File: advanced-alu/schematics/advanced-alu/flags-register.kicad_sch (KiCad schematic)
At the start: 2 parts

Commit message: updated ALU design
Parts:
- added U?: 74LS04, symbol 74xx:74LS04
- added U?: 74LS245, symbol 74xx:74LS245
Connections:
- net CF: now also U?.3 (A1)
- net EF: now also U?.5 (A3)
- net GND: now also U?.10 (GND), U?.6 (A4), U?.7 (A5), U?.8 (A6), U?.9 (A7)
- net OF: now also U?.4 (A2)
- net VCC: now also U?.1 (A->B), U?.20 (VCC)
- net ZF: now also U?.2 (A0)
- net ∑f renamed ALUf
- new net: U?.19 (CE), U?.2
- new net BUS_0: U?.18 (B0)
- new net BUS_1: U?.17 (B1)
- new net BUS_2: U?.16 (B2)
- new net BUS_3: U?.15 (B3)
- new net BUS_4: U?.14 (B4)
- new net BUS_5: U?.13 (B5)
- new net BUS_6: U?.12 (B6)
- new net BUS_7: U?.11 (B7)
- new net Fo: U?.1

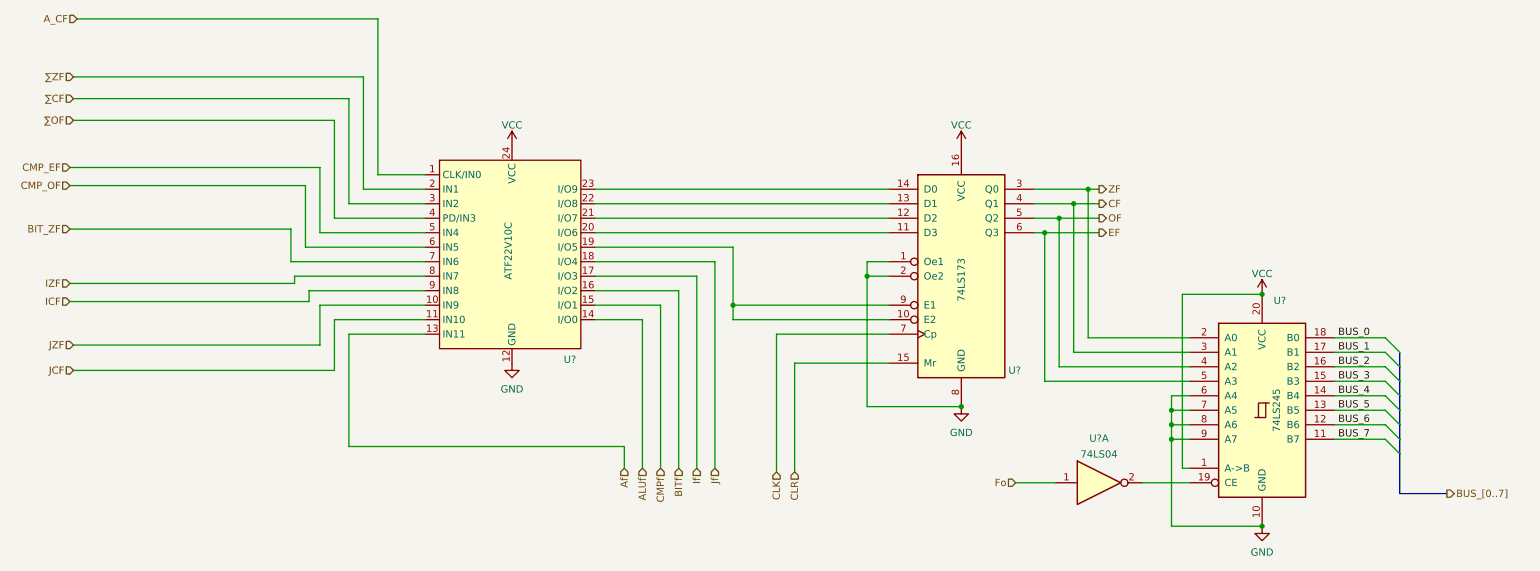
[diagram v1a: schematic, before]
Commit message: updated flags register
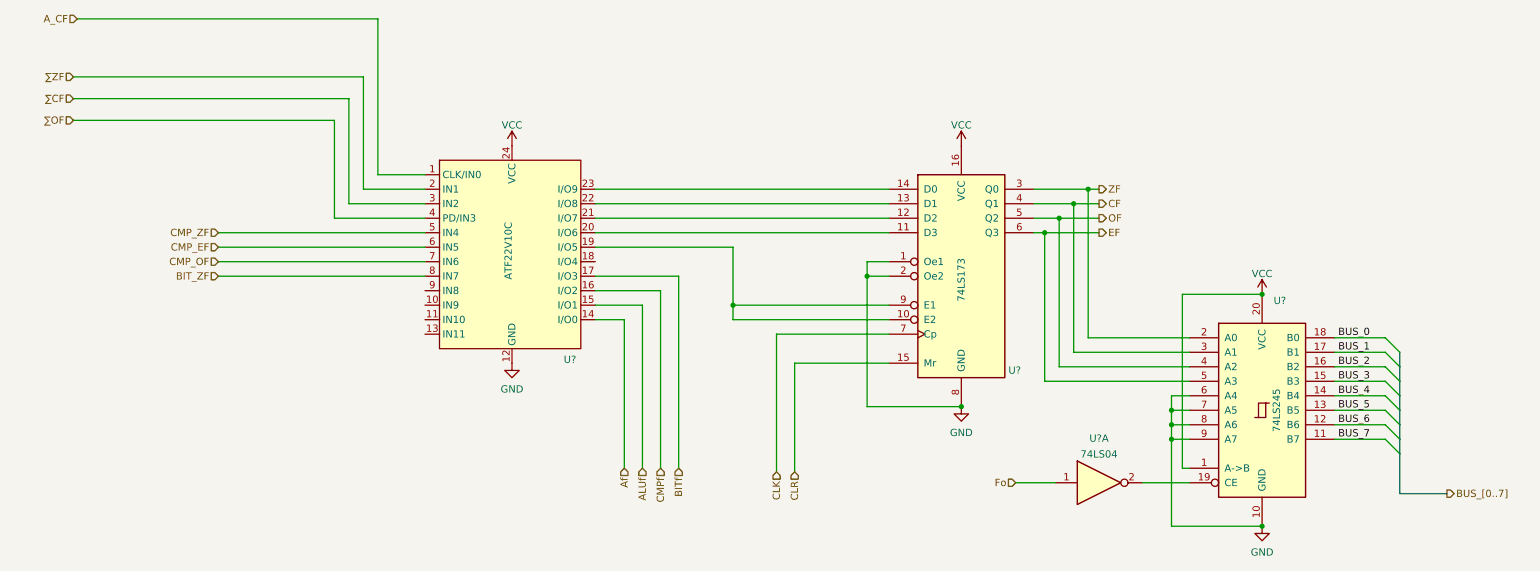
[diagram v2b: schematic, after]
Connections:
- net IZF is gone; now on net BIT_ZF: U?.8 (IN7)
- net If is gone; now on net BITf: U?.17 (I/O3)
- net ALUf: now also U?.15 (I/O1); no longer U?.14 (I/O0)
- net Af: now also U?.14 (I/O0); no longer U?.13 (IN11)
- net BIT_ZF: no longer U?.7 (IN6)
- net BITf: no longer U?.16 (I/O2)
- net CMP_EF: now also U?.6 (IN5); no longer U?.5 (IN4)
- net CMP_OF: now also U?.7 (IN6); no longer U?.6 (IN5)
- net CMPf: now also U?.16 (I/O2); no longer U?.15 (I/O1)
- net ICF: no longer names the net of U?.9 (IN8)
- net JCF: no longer names the net of U?.11 (IN10)
- net JZF: no longer names the net of U?.10 (IN9)
- net Jf: no longer names the net of U?.18 (I/O4)
- new net CMP_ZF: U?.5 (IN4)

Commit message: updated documentation
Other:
- title: (none) -> Advanced Arithmetic Logic Unit - Flags Register
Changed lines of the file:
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@@
 (kicad_sch (version 20211123) (generator eeschema)
   (paper "A4")
+  (title_block
+    (title "Advanced Arithmetic Logic Unit - Flags Register")
+  )
   (junction (at 217.17 119.38) (diameter 0) (color 0 0 0 0)
   )

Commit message: returned temp registr to being 8-bit
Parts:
- gave numbers to parts that had none: 4
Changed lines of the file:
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@@
   (symbol (lib_id "74xx:74LS04") (at 204.47 127 0) (unit 1)
     (in_bom yes) (on_board yes) (fields_autoplaced)
-    (property "Reference" "U?" (id 0) (at 204.47 119.2235 0))
+    (property "Reference" "U26" (id 0) (at 204.47 119.2235 0))
     (property "Value" "74LS04" (id 1) (at 204.47 121.9986 0))
     (property "Footprint" "" (id 2) (at 204.47 127 0)
@@
   (symbol (lib_id "power:GND") (at 101.6 106.045 0) (unit 1)
     (in_bom yes) (on_board yes) (fields_autoplaced)
-    (property "Reference" "#PWR?" (id 0) (at 101.6 112.395 0)
+    (property "Reference" "#PWR030" (id 0) (at 101.6 112.395 0)
       (effects (font (size 1.27 1.27)) hide)
     )
@@
   (symbol (lib_id "power:VCC") (at 233.045 93.98 0) (unit 1)
     (in_bom yes) (on_board yes) (fields_autoplaced)
-    (property "Reference" "#PWR?" (id 0) (at 233.045 97.79 0)
+    (property "Reference" "#PWR033" (id 0) (at 233.045 97.79 0)
       (effects (font (size 1.27 1.27)) hide)
     )
@@
   (symbol (lib_id "power:GND") (at 180.34 113.665 0) (unit 1)
     (in_bom yes) (on_board yes) (fields_autoplaced)
-    (property "Reference" "#PWR?" (id 0) (at 180.34 120.015 0)
+    (property "Reference" "#PWR032" (id 0) (at 180.34 120.015 0)
       (effects (font (size 1.27 1.27)) hide)
     )
@@
   (symbol (lib_id "power:GND") (at 233.045 134.62 0) (unit 1)
     (in_bom yes) (on_board yes) (fields_autoplaced)
-    (property "Reference" "#PWR?" (id 0) (at 233.045 140.97 0)
+    (property "Reference" "#PWR034" (id 0) (at 233.045 140.97 0)
       (effects (font (size 1.27 1.27)) hide)
     )
@@
   (symbol (lib_id "power:VCC") (at 101.6 67.945 0) (unit 1)
     (in_bom yes) (on_board yes) (fields_autoplaced)
-    (property "Reference" "#PWR?" (id 0) (at 101.6 71.755 0)
+    (property "Reference" "#PWR029" (id 0) (at 101.6 71.755 0)
       (effects (font (size 1.27 1.27)) hide)
     )
@@
   (symbol (lib_id "74xx:74LS173") (at 180.34 90.805 0) (unit 1)
     (in_bom yes) (on_board yes)
-    (property "Reference" "U?" (id 0) (at 188.595 107.315 0)
+    (property "Reference" "U25" (id 0) (at 188.595 107.315 0)
       (effects (font (size 1.27 1.27)) (justify left))
     )
@@
   (symbol (lib_id "power:VCC") (at 180.34 67.945 0) (unit 1)
     (in_bom yes) (on_board yes) (fields_autoplaced)
-    (property "Reference" "#PWR?" (id 0) (at 180.34 71.755 0)
+    (property "Reference" "#PWR031" (id 0) (at 180.34 71.755 0)
       (effects (font (size 1.27 1.27)) hide)
     )
@@
   (symbol (lib_id "74xx:74LS245") (at 233.045 114.3 0) (unit 1)
     (in_bom yes) (on_board yes)
-    (property "Reference" "U?" (id 0) (at 235.0644 95.0935 0)
+    (property "Reference" "U27" (id 0) (at 235.0644 95.0935 0)
       (effects (font (size 1.27 1.27)) (justify left))
     )
@@
   (symbol (lib_id "common-symbols:ATF22V10C") (at 101.6 86.995 0) (unit 1)
     (in_bom yes) (on_board yes)
-    (property "Reference" "U?" (id 0) (at 111.76 105.41 0))
+    (property "Reference" "U24" (id 0) (at 111.76 105.41 0))
     (property "Value" "ATF22V10C" (id 1) (at 100.965 86.36 90))
     (property "Footprint" "" (id 2) (at 101.6 86.995 0)

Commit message: small changes toimprove layout
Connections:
- net ALUf: now also U24.10 (IN9); no longer U24.15 (I/O1)
- net Af: now also U24.9 (IN8); no longer U24.14 (I/O0)
- net BITf: now also U24.13 (IN11); no longer U24.17 (I/O3)
- net CMPf: now also U24.11 (IN10); no longer U24.16 (I/O2)
- no-connect marks 0 -> 5
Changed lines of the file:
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@@
   (junction (at 217.17 116.84) (diameter 0) (color 0 0 0 0)
   )
+  (no_connect (at 116.205 88.265))
+  (no_connect (at 116.205 90.805))
+  (no_connect (at 116.205 93.345))
+  (no_connect (at 116.205 95.885))
+  (no_connect (at 116.205 98.425))
   (bus_entry (at 254.635 104.14) (size 2.54 2.54)
     (stroke (width 0) (type default) (color 0 0 0 0))
@@
     (stroke (width 0) (type default) (color 0 0 0 0))
   )
-  (wire (pts (xy 73.025 78.105) (xy 86.36 78.105))
+  (wire (pts (xy 50.165 78.105) (xy 86.36 78.105))
     (stroke (width 0) (type default) (color 0 0 0 0))
   )
@@
     (stroke (width 0) (type default) (color 0 0 0 0))
   )
-  (wire (pts (xy 70.485 80.645) (xy 86.36 80.645))
+  (wire (pts (xy 50.165 80.645) (xy 86.36 80.645))
     (stroke (width 0) (type default) (color 0 0 0 0))
   )
@@
     (stroke (width 0) (type default) (color 0 0 0 0))
   )
-  (wire (pts (xy 75.565 55.88) (xy 75.565 75.565))
+  (wire (pts (xy 50.165 98.425) (xy 86.36 98.425))
     (stroke (width 0) (type default) (color 0 0 0 0))
   )
@@
     (stroke (width 0) (type default) (color 0 0 0 0))
   )
-  (wire (pts (xy 130.81 90.805) (xy 130.81 124.46))
-    (stroke (width 0) (type default) (color 0 0 0 0))
-  )
-  (wire (pts (xy 24.765 55.88) (xy 75.565 55.88))
-    (stroke (width 0) (type default) (color 0 0 0 0))
-  )
   (wire (pts (xy 163.83 90.805) (xy 163.83 113.665))
     (stroke (width 0) (type default) (color 0 0 0 0))
@@
     (stroke (width 0) (type default) (color 0 0 0 0))
   )
+  (wire (pts (xy 50.165 100.965) (xy 86.36 100.965))
+    (stroke (width 0) (type default) (color 0 0 0 0))
+  )
   (wire (pts (xy 217.17 116.84) (xy 217.17 119.38))
     (stroke (width 0) (type default) (color 0 0 0 0))
@@
     (stroke (width 0) (type default) (color 0 0 0 0))
   )
-  (wire (pts (xy 127.635 93.345) (xy 127.635 124.46))
-    (stroke (width 0) (type default) (color 0 0 0 0))
-  )
   (wire (pts (xy 189.865 127) (xy 196.85 127))
     (stroke (width 0) (type default) (color 0 0 0 0))
   )
-  (wire (pts (xy 121.285 98.425) (xy 116.205 98.425))
-    (stroke (width 0) (type default) (color 0 0 0 0))
-  )
   (wire (pts (xy 220.345 124.46) (xy 219.075 124.46))
     (stroke (width 0) (type default) (color 0 0 0 0))
@@
     (stroke (width 0) (type default) (color 0 0 0 0))
   )
-  (wire (pts (xy 78.105 73.025) (xy 86.36 73.025))
+  (wire (pts (xy 50.165 73.025) (xy 86.36 73.025))
     (stroke (width 0) (type default) (color 0 0 0 0))
   )
@@
     (stroke (width 0) (type default) (color 0 0 0 0))
   )
-  (wire (pts (xy 121.285 98.425) (xy 121.285 124.46))
-    (stroke (width 0) (type default) (color 0 0 0 0))
-  )
   (wire (pts (xy 200.025 78.105) (xy 204.47 78.105))
     (stroke (width 0) (type default) (color 0 0 0 0))
@@
     (stroke (width 0) (type default) (color 0 0 0 0))
   )
-  (wire (pts (xy 73.025 59.69) (xy 73.025 78.105))
-    (stroke (width 0) (type default) (color 0 0 0 0))
-  )
   (bus (pts (xy 257.175 114.3) (xy 257.175 116.84))
     (stroke (width 0) (type default) (color 0 0 0 0))
@@
     (stroke (width 0) (type default) (color 0 0 0 0))
   )
-  (wire (pts (xy 24.765 63.5) (xy 70.485 63.5))
-    (stroke (width 0) (type default) (color 0 0 0 0))
-  )
-  (wire (pts (xy 124.46 95.885) (xy 116.205 95.885))
-    (stroke (width 0) (type default) (color 0 0 0 0))
-  )
   (wire (pts (xy 167.64 90.805) (xy 163.83 90.805))
     (stroke (width 0) (type default) (color 0 0 0 0))
   )
-  (wire (pts (xy 78.105 45.72) (xy 78.105 73.025))
-    (stroke (width 0) (type default) (color 0 0 0 0))
-  )
   (wire (pts (xy 220.345 116.84) (xy 217.17 116.84))
     (stroke (width 0) (type default) (color 0 0 0 0))
@@
     (stroke (width 0) (type default) (color 0 0 0 0))
   )
-  (wire (pts (xy 124.46 95.885) (xy 124.46 124.46))
-    (stroke (width 0) (type default) (color 0 0 0 0))
-  )
   (wire (pts (xy 219.075 124.46) (xy 219.075 93.98))
     (stroke (width 0) (type default) (color 0 0 0 0))
@@
     (stroke (width 0) (type default) (color 0 0 0 0))
   )
+  (wire (pts (xy 50.165 93.345) (xy 86.36 93.345))
+    (stroke (width 0) (type default) (color 0 0 0 0))
+  )
+  (wire (pts (xy 50.165 95.885) (xy 86.36 95.885))
+    (stroke (width 0) (type default) (color 0 0 0 0))
+  )
   (wire (pts (xy 116.205 75.565) (xy 167.64 75.565))
     (stroke (width 0) (type default) (color 0 0 0 0))
   )
-  (wire (pts (xy 127.635 93.345) (xy 116.205 93.345))
-    (stroke (width 0) (type default) (color 0 0 0 0))
-  )
   (wire (pts (xy 245.745 109.22) (xy 254.635 109.22))
     (stroke (width 0) (type default) (color 0 0 0 0))
   )
-  (wire (pts (xy 24.765 59.69) (xy 73.025 59.69))
-    (stroke (width 0) (type default) (color 0 0 0 0))
-  )
-  (wire (pts (xy 130.81 90.805) (xy 116.205 90.805))
-    (stroke (width 0) (type default) (color 0 0 0 0))
-  )
   (bus (pts (xy 257.175 106.68) (xy 257.175 109.22))
     (stroke (width 0) (type default) (color 0 0 0 0))
   )
-  (wire (pts (xy 75.565 75.565) (xy 86.36 75.565))
-    (stroke (width 0) (type default) (color 0 0 0 0))
-  )
-  (wire (pts (xy 25.4 45.72) (xy 78.105 45.72))
+  (wire (pts (xy 50.165 75.565) (xy 86.36 75.565))
     (stroke (width 0) (type default) (color 0 0 0 0))
   )
@@
     (stroke (width 0) (type default) (color 0 0 0 0))
   )
-  (wire (pts (xy 70.485 63.5) (xy 70.485 80.645))
-    (stroke (width 0) (type default) (color 0 0 0 0))
-  )
   (label "BUS_4" (at 246.38 111.76 0)
     (effects (font (size 1.27 1.27)) (justify left bottom))
@@
     (effects (font (size 1.27 1.27)) (justify left))
   )
-  (hierarchical_label "A_CF" (shape input) (at 25.4 45.72 180)
-    (effects (font (size 1.27 1.27)) (justify right))
-  )
-  (hierarchical_label "∑ZF" (shape input) (at 24.765 55.88 180)
+  (hierarchical_label "A_CF" (shape input) (at 50.165 73.025 180)
+    (effects (font (size 1.27 1.27)) (justify right))
+  )
+  (hierarchical_label "∑ZF" (shape input) (at 50.165 75.565 180)
     (effects (font (size 1.27 1.27)) (justify right))
   )
@@
     (effects (font (size 1.27 1.27)) (justify left))
   )
-  (hierarchical_label "BITf" (shape input) (at 130.81 124.46 270)
+  (hierarchical_label "BITf" (shape input) (at 50.165 100.965 180)
     (effects (font (size 1.27 1.27)) (justify right))
   )
@@
     (effects (font (size 1.27 1.27)) (justify left))
   )
-  (hierarchical_label "Af" (shape input) (at 121.285 124.46 270)
-    (effects (font (size 1.27 1.27)) (justify right))
-  )
-  (hierarchical_label "CMPf" (shape input) (at 127.635 124.46 270)
+  (hierarchical_label "Af" (shape input) (at 50.165 93.345 180)
+    (effects (font (size 1.27 1.27)) (justify right))
+  )
+  (hierarchical_label "CMPf" (shape input) (at 50.165 98.425 180)
     (effects (font (size 1.27 1.27)) (justify right))
   )
@@
     (effects (font (size 1.27 1.27)) (justify right))
   )
-  (hierarchical_label "∑OF" (shape input) (at 24.765 63.5 180)
-    (effects (font (size 1.27 1.27)) (justify right))
-  )
-  (hierarchical_label "ALUf" (shape input) (at 124.46 124.46 270)
+  (hierarchical_label "∑OF" (shape input) (at 50.165 80.645 180)
+    (effects (font (size 1.27 1.27)) (justify right))
+  )
+  (hierarchical_label "ALUf" (shape input) (at 50.165 95.885 180)
     (effects (font (size 1.27 1.27)) (justify right))
   )
@@
     (effects (font (size 1.27 1.27)) (justify right))
   )
-  (hierarchical_label "∑CF" (shape input) (at 24.765 59.69 180)
+  (hierarchical_label "∑CF" (shape input) (at 50.165 78.105 180)
     (effects (font (size 1.27 1.27)) (justify right))
   )
@@
     (pin "1")
     (pin "2")
-    (pin "3")
-    (pin "4")
-    (pin "5")
-    (pin "6")
-    (pin "8")
-    (pin "9")
-    (pin "10")
-    (pin "11")
-    (pin "12")
-    (pin "13")
-    (pin "14")
-    (pin "7")
   )
   (symbol (lib_id "power:GND") (at 101.6 106.045 0) (unit 1)

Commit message: tweaks and layout improvements
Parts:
- renumbered U24 to U25, U25 to U26, U26 to U27, U27 to U28
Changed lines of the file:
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@@
   (symbol (lib_id "74xx:74LS04") (at 204.47 127 0) (unit 1)
     (in_bom yes) (on_board yes) (fields_autoplaced)
-    (property "Reference" "U26" (id 0) (at 204.47 119.2235 0))
+    (property "Reference" "U27" (id 0) (at 204.47 119.2235 0))
     (property "Value" "74LS04" (id 1) (at 204.47 121.9986 0))
     (property "Footprint" "" (id 2) (at 204.47 127 0)
@@
     (pin "1")
     (pin "2")
-    (pin "3")
-    (pin "4")
-    (pin "5")
-    (pin "6")
-    (pin "8")
-    (pin "9")
-    (pin "10")
-    (pin "11")
-    (pin "12")
-    (pin "13")
-    (pin "14")
-    (pin "7")
   )
   (symbol (lib_id "power:GND") (at 101.6 106.045 0) (unit 1)
     (in_bom yes) (on_board yes) (fields_autoplaced)
-    (property "Reference" "#PWR030" (id 0) (at 101.6 112.395 0)
+    (property "Reference" "#PWR034" (id 0) (at 101.6 112.395 0)
       (effects (font (size 1.27 1.27)) hide)
     )
@@
   (symbol (lib_id "power:VCC") (at 233.045 93.98 0) (unit 1)
     (in_bom yes) (on_board yes) (fields_autoplaced)
-    (property "Reference" "#PWR033" (id 0) (at 233.045 97.79 0)
+    (property "Reference" "#PWR037" (id 0) (at 233.045 97.79 0)
       (effects (font (size 1.27 1.27)) hide)
     )
@@
   (symbol (lib_id "power:GND") (at 180.34 113.665 0) (unit 1)
     (in_bom yes) (on_board yes) (fields_autoplaced)
-    (property "Reference" "#PWR032" (id 0) (at 180.34 120.015 0)
+    (property "Reference" "#PWR036" (id 0) (at 180.34 120.015 0)
       (effects (font (size 1.27 1.27)) hide)
     )
@@
   (symbol (lib_id "power:GND") (at 233.045 134.62 0) (unit 1)
     (in_bom yes) (on_board yes) (fields_autoplaced)
-    (property "Reference" "#PWR034" (id 0) (at 233.045 140.97 0)
+    (property "Reference" "#PWR038" (id 0) (at 233.045 140.97 0)
       (effects (font (size 1.27 1.27)) hide)
     )
@@
   (symbol (lib_id "power:VCC") (at 101.6 67.945 0) (unit 1)
     (in_bom yes) (on_board yes) (fields_autoplaced)
-    (property "Reference" "#PWR029" (id 0) (at 101.6 71.755 0)
+    (property "Reference" "#PWR033" (id 0) (at 101.6 71.755 0)
       (effects (font (size 1.27 1.27)) hide)
     )
@@
   (symbol (lib_id "74xx:74LS173") (at 180.34 90.805 0) (unit 1)
     (in_bom yes) (on_board yes)
-    (property "Reference" "U25" (id 0) (at 188.595 107.315 0)
+    (property "Reference" "U26" (id 0) (at 188.595 107.315 0)
       (effects (font (size 1.27 1.27)) (justify left))
     )
@@
   (symbol (lib_id "power:VCC") (at 180.34 67.945 0) (unit 1)
     (in_bom yes) (on_board yes) (fields_autoplaced)
-    (property "Reference" "#PWR031" (id 0) (at 180.34 71.755 0)
+    (property "Reference" "#PWR035" (id 0) (at 180.34 71.755 0)
       (effects (font (size 1.27 1.27)) hide)
     )
@@
   (symbol (lib_id "74xx:74LS245") (at 233.045 114.3 0) (unit 1)
     (in_bom yes) (on_board yes)
-    (property "Reference" "U27" (id 0) (at 235.0644 95.0935 0)
+    (property "Reference" "U28" (id 0) (at 235.0644 95.0935 0)
       (effects (font (size 1.27 1.27)) (justify left))
     )
@@
   (symbol (lib_id "common-symbols:ATF22V10C") (at 101.6 86.995 0) (unit 1)
     (in_bom yes) (on_board yes)
-    (property "Reference" "U24" (id 0) (at 111.76 105.41 0))
+    (property "Reference" "U25" (id 0) (at 111.76 105.41 0))
     (property "Value" "ATF22V10C" (id 1) (at 100.965 86.36 90))
     (property "Footprint" "" (id 2) (at 101.6 86.995 0)

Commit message: corrected control lines
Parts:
- renumbered U25 to U26, U26 to U27, U27 to U28, U28 to U29
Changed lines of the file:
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@@
   (symbol (lib_id "74xx:74LS04") (at 204.47 127 0) (unit 1)
     (in_bom yes) (on_board yes) (fields_autoplaced)
-    (property "Reference" "U27" (id 0) (at 204.47 119.2235 0))
+    (property "Reference" "U28" (id 0) (at 204.47 119.2235 0))
     (property "Value" "74LS04" (id 1) (at 204.47 121.9986 0))
     (property "Footprint" "" (id 2) (at 204.47 127 0)
@@
   (symbol (lib_id "74xx:74LS173") (at 180.34 90.805 0) (unit 1)
     (in_bom yes) (on_board yes)
-    (property "Reference" "U26" (id 0) (at 188.595 107.315 0)
+    (property "Reference" "U27" (id 0) (at 188.595 107.315 0)
       (effects (font (size 1.27 1.27)) (justify left))
     )
@@
   (symbol (lib_id "74xx:74LS245") (at 233.045 114.3 0) (unit 1)
     (in_bom yes) (on_board yes)
-    (property "Reference" "U28" (id 0) (at 235.0644 95.0935 0)
+    (property "Reference" "U29" (id 0) (at 235.0644 95.0935 0)
       (effects (font (size 1.27 1.27)) (justify left))
     )
@@
   (symbol (lib_id "common-symbols:ATF22V10C") (at 101.6 86.995 0) (unit 1)
     (in_bom yes) (on_board yes)
-    (property "Reference" "U25" (id 0) (at 111.76 105.41 0))
+    (property "Reference" "U26" (id 0) (at 111.76 105.41 0))
     (property "Value" "ATF22V10C" (id 1) (at 100.965 86.36 90))
     (property "Footprint" "" (id 2) (at 101.6 86.995 0)
